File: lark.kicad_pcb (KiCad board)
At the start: 2 copper layers, 128 parts, among them CON1 SJ1-3523N, IC1 MS5611-01BA03, IC2 MS5611-01BA03, J1 SPI, J2 UART0, J3 I2C_0, J4 PWR_IN, J5 UE27AC54100, J6 UART1, J7 54602-908LF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

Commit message: Intermediate status while arranging compontents.
Manually grouped components into smaller islands.

Some parts were changed:
* U1: SOT-23-3 LDO should be sufficient
* CP_Elec: Use 10x10 size
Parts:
- C10, C16, C46: footprint Capacitor_SMD:CP_Elec_16x17.5 -> Capacitor_SMD:CP_Elec_10x10
- D3, D5: footprint Diode_SMD:D_SMC_Handsoldering -> Diode_SMD:D_SOD-123
- D4: footprint Diode_SMD:D_SMB_Handsoldering -> Diode_SMD:D_SOD-123
- J5: moved to B.Cu
- U1: value AP1117-33 -> MCP1700T-3302E_TT; footprint Package_TO_SOT_SMD:SOT-223-3_TabPin2 -> Package_TO_SOT_SMD:SOT-23
- U3, U4, U5, U6: footprint digikey-footprints:SOT-23-3 -> Package_TO_SOT_SMD:SOT-23
- moved C11 245.2 mm to (234.0, -23.0)
- moved C12 243.8 mm to (234.0, -27.0)
- moved C45 230.0 mm to (152.0, -50.0)
- moved C44 225.1 mm to (152.0, -54.0)
- moved C7 223.6 mm to (244.0, 119.0)
- moved R24 219.5 mm to (244.0, 122.0)
- moved C47 212.7 mm to (128.0, -56.5)
- moved R33 212.7 mm to (124.3, -54.5)
- moved R29 204.9 mm to (134.0, -46.0)
- moved R36 202.1 mm to (129.0, -50.0)
- moved C17 201.9 mm to (245.0, 63.0)
- moved C49 200.9 mm to (135.0, -50.0)
- moved R35 197.2 mm to (133.0, -38.0)
- moved R34 183.8 mm to (133.0, -41.0)
- moved U1 179.2 mm to (4.00, 70.0)
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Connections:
- IC1 pad 7: I2C1_SDA -> I2C0_SDA
- IC1 pad 8: I2C1_SCK -> I2C0_SCK
- IC2 pad 5: GND -> /Power/PDUSPWR
- U9 pad 6: I2C0_SDA -> I2C1_SDA
- U9 pad 7: I2C0_SCK -> I2C1_SCK

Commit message: continue layout work, WIP
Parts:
- moved J4 236.4 mm to (5.64, 7.74), turned to 270 degrees
- moved C10 236.0 mm to (7.00, -4.00), turned to 270 degrees
- moved D4 232.7 mm to (12.6, 5.74), turned to 180 degrees
- moved L1 230.2 mm to (17.6, -1.36)
- moved C9 227.7 mm to (20.6, -3.33)
- moved D3 225.7 mm to (18.6, 5.74), turned to 180 degrees
- moved RV1 225.1 mm to (15.4, 11.2), turned to 180 degrees
- moved C12 222.2 mm to (13.6, 1.62), turned to 270 degrees
- moved C8 222.1 mm to (20.6, 1.64), turned to 270 degrees
- moved C11 221.2 mm to (13.6, -3.36), turned to 90 degrees
- moved U2 212.4 mm to (28.0, 2.38), turned to 90 degrees
- moved C16 208.6 mm to (42.0, -5.00)
- moved D5 206.4 mm to (51.0, 6.00), turned to 90 degrees
- moved C17 204.4 mm to (51.0, -1.26), turned to 90 degrees
- moved L3 204.2 mm to (42.0, 8.00), turned to 180 degrees
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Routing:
- net I2C0_SCK: track 0.00 -> 44.7 mm
- net I2C0_SDA: track 0.00 -> 43.8 mm
- net I2C1_SCK: track 0.00 -> 24.8 mm
- net I2C1_SDA: track 0.00 -> 16.5 mm
- net BOOTM: track 0.00 -> 15.1 mm, vias 0 -> 1
- net SPICS0: track 0.00 -> 14.2 mm, vias 0 -> 1
- net U1TXD: track 0.00 -> 12.5 mm
- net U0RXD: track 0.00 -> 11.6 mm, vias 0 -> 1
- net SW_VARIO: track 0.00 -> 10.5 mm, vias 0 -> 1
- net U1RTS: track 0.00 -> 8.74 mm
- net SPID: track 0.00 -> 8.72 mm
- net U2TXD: track 0.00 -> 8.57 mm
- net SPIQ: track 0.00 -> 7.39 mm
- net U1CTS: track 0.00 -> 7.16 mm
- net SPICLK: track 0.00 -> 7.14 mm
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
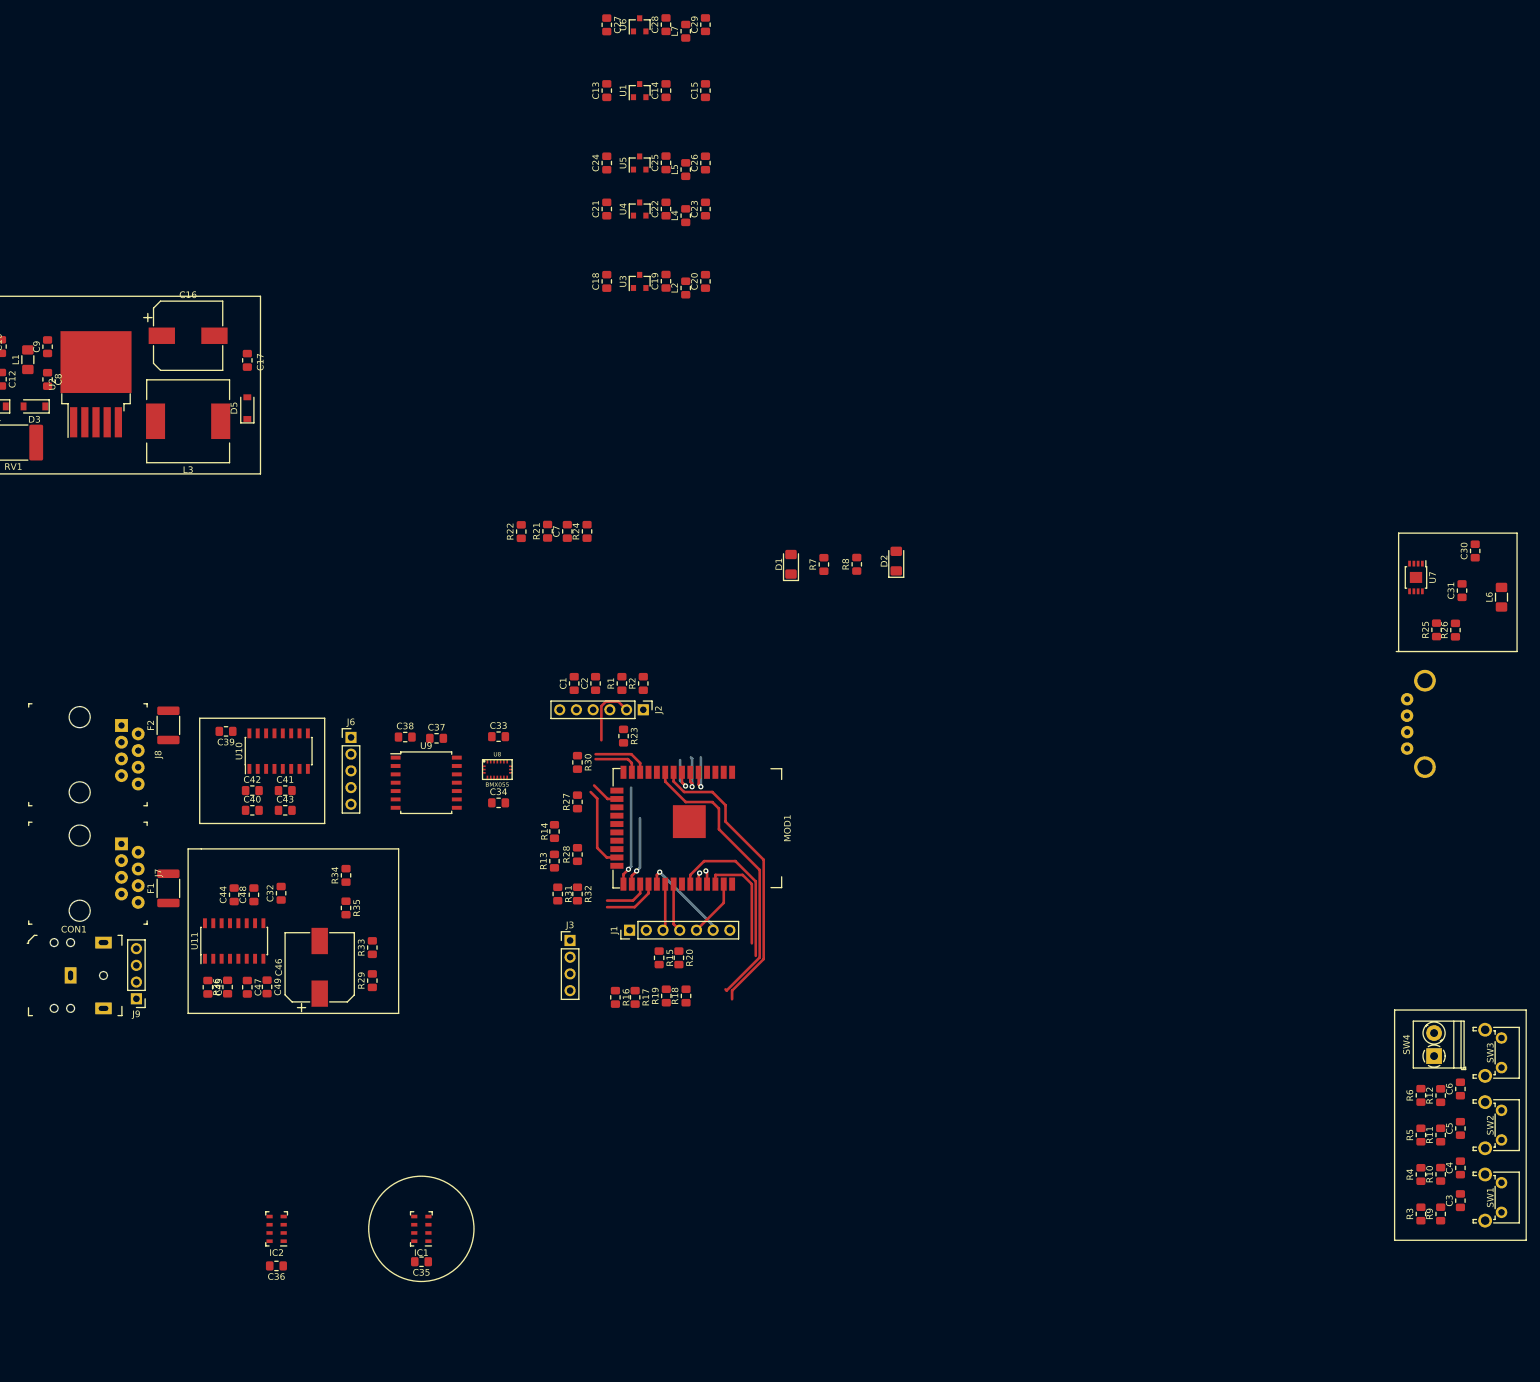
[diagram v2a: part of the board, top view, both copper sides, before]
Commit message: Updating schematic for the first prototype
* U1 can supply up to 600 mA
* drop USB charger for now
* smaller type of DC/DC (U2) for input
* remove one of the large capacitors
* change BMX interface to 4-wire SPI for speed reasons
* add I2C mux for pressure sensors

The changes were made during the meeting with Tomas.

BMX055 will be replaced by BMX088. For mechanical reasons, the pressure
sensors will be placed on a daughterboard. The daughterboard could get
footprints for different kinds pressure sensors (i.e. BMP388, HCLA0025).
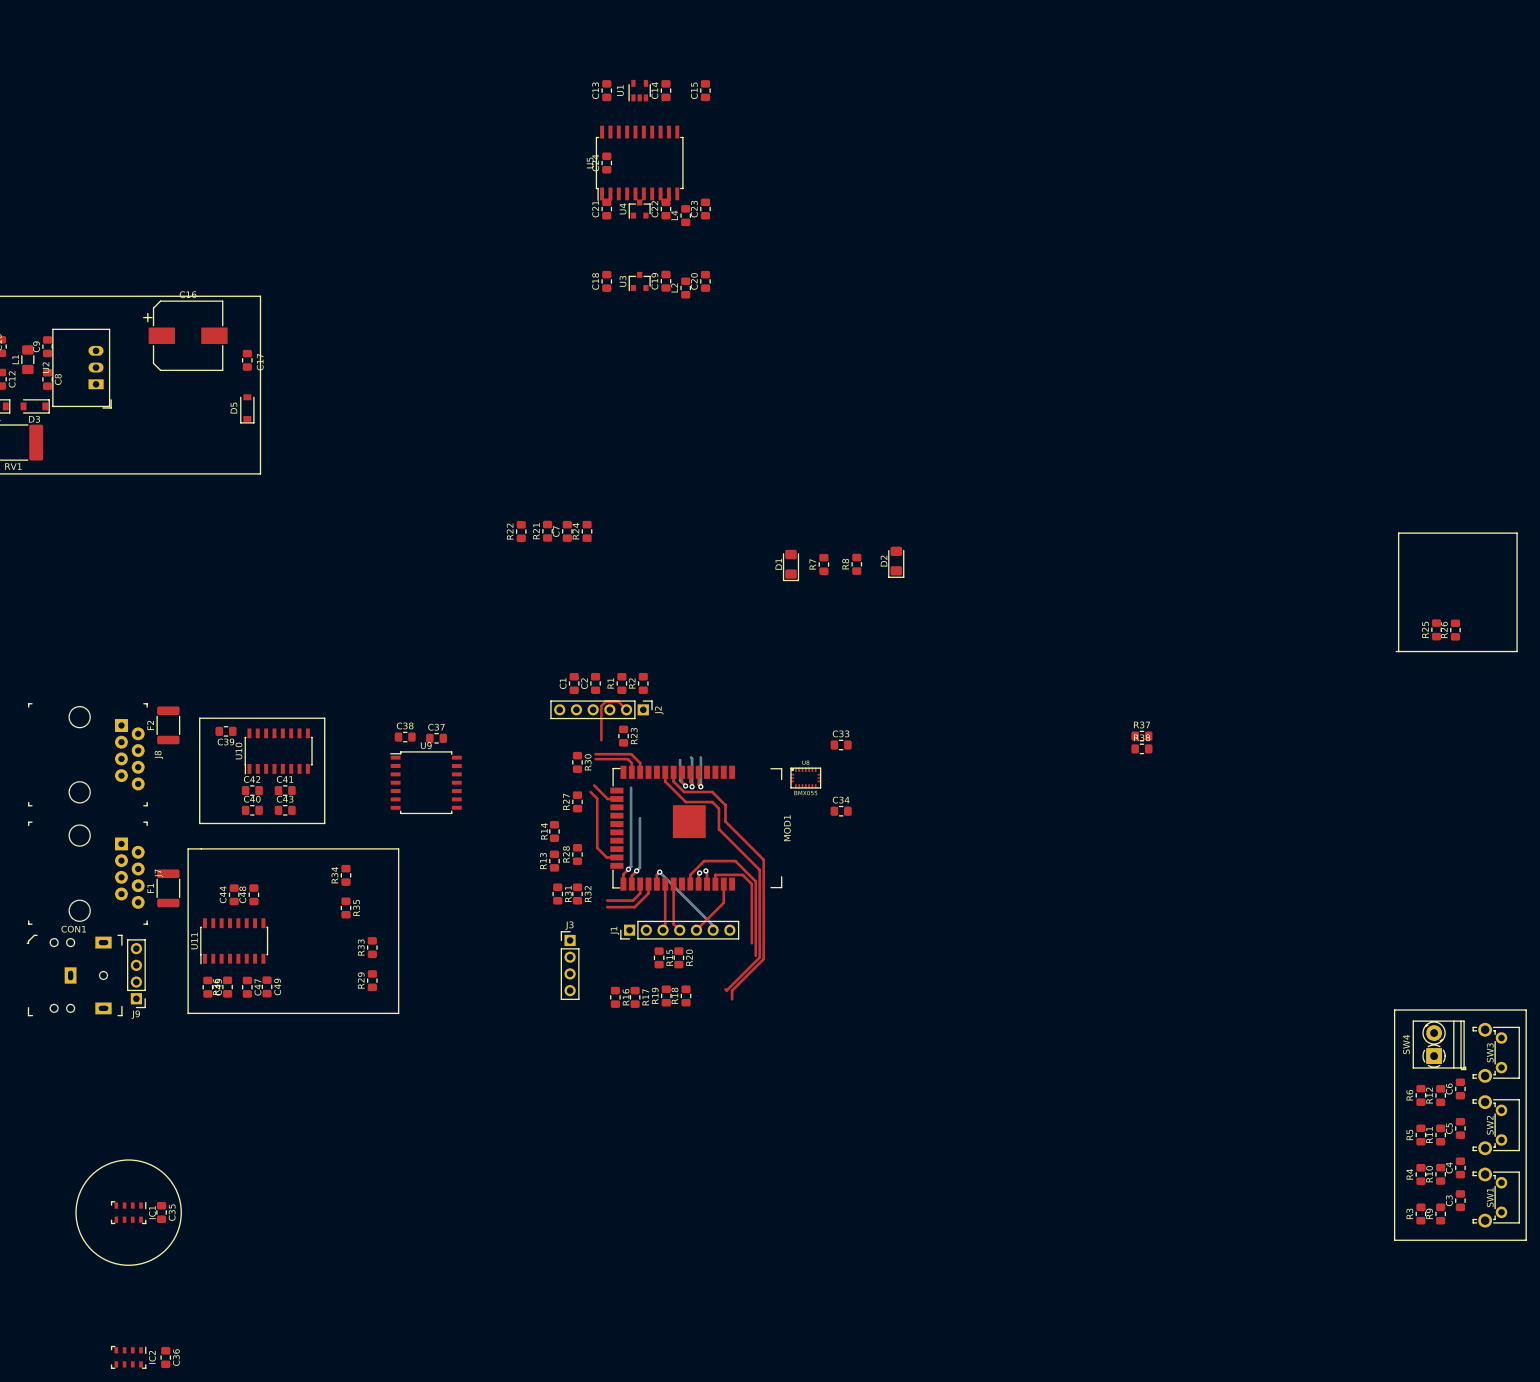
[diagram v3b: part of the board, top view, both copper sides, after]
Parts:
- removed C25, C26, C27, C28, C29, C31: 1u, Capacitor_SMD:C_0805_2012Metric_Pad1.15x1.40mm_HandSolder
- removed C30, C32: 100n, Capacitor_SMD:C_0805_2012Metric_Pad1.15x1.40mm_HandSolder
- removed C46: 470u, Capacitor_SMD:CP_Elec_10x10
- removed J5: UE27AC54100, digikey-footprints:USB_A_Female_UE27AC54100
- removed J6: UART1, Connector_PinHeader_2.54mm:PinHeader_1x05_P2.54mm_Vertical
- removed L3: 47uH/3.5A, Inductor_SMD:L_12x12mm_H8mm
- removed L5, L7: Ferrite_Bead, Inductor_SMD:L_0805_2012Metric_Pad1.15x1.40mm_HandSolder
- removed L6: Ferrite_Bead, Inductor_SMD:L_1206_3216Metric_Pad1.42x1.75mm_HandSolder
- removed U6: MCP1700T-3302E_TT, Package_TO_SOT_SMD:SOT-23
- removed U7: TPS2511, Package_SO:MSOP-8-1EP_3x3mm_P0.65mm_EP1.68x1.88mm
- added R37: 10k, Resistor_SMD:R_0805_2012Metric_Pad1.15x1.40mm_HandSolder, F.Cu at (187.0, 55.9)
- added R38: 10k, Resistor_SMD:R_0805_2012Metric_Pad1.15x1.40mm_HandSolder, F.Cu at (187.0, 57.8)
- C24: value 1u -> 100n
- R26: value 22k -> 10k
- R29, R30: value 470R -> 10k
- U1: value MCP1700T-3302E_TT -> AP2112K-3.3; footprint Package_TO_SOT_SMD:SOT-23 -> Package_TO_SOT_SMD:SOT-23-5
- U2: value LM2596S-5 -> R-785.0-1.0; footprint Package_TO_SOT_SMD:TO-263-5_TabPin3 -> Converter_DCDC:Converter_DCDC_RECOM_R-78E-0.5_THT
- U5: value MCP1700T-3302E_TT -> PCA9544AD; footprint Package_TO_SOT_SMD:SOT-23 -> Package_SO:SOIC-20W_7.5x12.8mm_P1.27mm
- moved C33 52.1 mm to (141.3, 57.2)
- moved C34 52.1 mm to (141.3, 67.3)
- moved U8 46.9 mm to (135.9, 62.2)
- moved IC1 44.6 mm to (33.0, 128.3), turned to 270 degrees
- moved C35 40.2 mm to (38.0, 128.3), turned to 270 degrees
- moved IC2 29.8 mm to (33.0, 150.3), turned to 270 degrees
- moved C36 21.8 mm to (38.6, 150.3), turned to 270 degrees
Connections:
- net Net-(U8-Pad16) renamed /Sensors/CS_ACC
- net Net-(U8-Pad5) renamed /Sensors/CS_GYR
- C23 pad 1: /Power/PSTATPWR -> /Power/SENSPWR
- C24 pad 1: +5V -> GND
- C24 pad 2: GND -> /Power/SENSPWR
- C35 pad 1: /Power/PSTATPWR -> GND
- C35 pad 2: GND -> /Power/SENSPWR
- C36 pad 1: /Power/PDUSPWR -> GND
- C36 pad 2: GND -> /Power/SENSPWR
- C37 pad 1: /Power/PDIFPWR -> /Power/SENSPWR
- C38 pad 1: /Power/PDIFPWR -> /Power/SENSPWR
- D5 pad 1: Net-(D5-Pad1) -> +12V
- D5 pad 2: GND -> +5V
- IC1 pad 1: /Power/PSTATPWR -> /Power/SENSPWR
- IC1 pad 2: /Power/PSTATPWR -> /Power/SENSPWR
- IC1 pad 4: GND -> /Power/SENSPWR
- IC1 pad 5: GND -> /Power/SENSPWR
- IC1 pad 7: I2C0_SDA -> Net-(IC1-Pad7)
- IC1 pad 8: I2C0_SCK -> Net-(IC1-Pad8)
- IC2 pad 1: /Power/PDUSPWR -> /Power/SENSPWR
- IC2 pad 2: /Power/PDUSPWR -> /Power/SENSPWR
- IC2 pad 4: GND -> /Power/SENSPWR
- IC2 pad 5: /Power/PDUSPWR -> /Power/SENSPWR
- IC2 pad 7: I2C0_SDA -> Net-(IC2-Pad7)
- IC2 pad 8: I2C0_SCK -> Net-(IC2-Pad8)
- L4 pad 1: /Power/PSTATPWR -> /Power/SENSPWR
- MOD1 pad 12: U1RTS -> INT_GYR
- MOD1 pad 13: U1CTS -> INT_ACC
- MOD1 pad 33: I2C1_SCK -> CS_ACC
- MOD1 pad 36: I2C1_SDA -> CS_GYR
- R16 pad 1: I2C1_SCK -> /Power/SENSPWR
- R16 pad 2: VDD -> Net-(R16-Pad2)
- R17 pad 1: I2C1_SDA -> /Power/SENSPWR
- R17 pad 2: VDD -> Net-(IC1-Pad7)
- R25 pad 1: Net-(R25-Pad1) -> /Power/SENSPWR
- R25 pad 2: +5V -> Net-(IC2-Pad7)
- R26 pad 1: Net-(R26-Pad1) -> /Power/SENSPWR
- R26 pad 2: GND -> Net-(R26-Pad2)
- R29 pad 1: Net-(J6-Pad3) -> /Power/SENSPWR
- R29 pad 2: U1RTS -> Net-(R29-Pad2)
- R30 pad 1: Net-(J6-Pad4) -> /Power/SENSPWR
- R30 pad 2: U1CTS -> Net-(IC1-Pad8)
- U1 pad 1: GND -> +5V
- U1 pad 2: VDD -> GND
- U2 pad 2: Net-(D5-Pad1) -> GND
- U2 pad 3: GND -> +5V
- U5 pad 2: Net-(C25-Pad1) -> GND
- U5 pad 3: +5V -> GND
- U8 pad 11: I2C1_SDA -> SPID
- U8 pad 12: GND -> SPIQ
- U8 pad 17: GND -> SPIQ
- U8 pad 20: GND -> Net-(U8-Pad20)
- U8 pad 9: I2C1_SCK -> SPICLK
- U9 pad 10: /Power/PDIFPWR -> /Power/SENSPWR
- U9 pad 11: /Power/PDIFPWR -> /Power/SENSPWR
- U9 pad 13: /Power/PDIFPWR -> /Power/SENSPWR
- U9 pad 6: I2C1_SDA -> Net-(R26-Pad2)
- U9 pad 7: I2C1_SCK -> Net-(R38-Pad2)
- U9 pad 8: /Power/PDIFPWR -> /Power/SENSPWR
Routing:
- net I2C1_SCK: track 24.8 -> 0.00 mm
- net CS_ACC: track 0.00 -> 24.8 mm
- net I2C1_SDA: track 16.5 -> 0.00 mm
- net CS_GYR: track 0.00 -> 16.5 mm
- net U1RTS: track 8.74 -> 0.00 mm
- net INT_GYR: track 0.00 -> 8.74 mm
- net U1CTS: track 7.16 -> 0.00 mm
- net INT_ACC: track 0.00 -> 7.16 mm

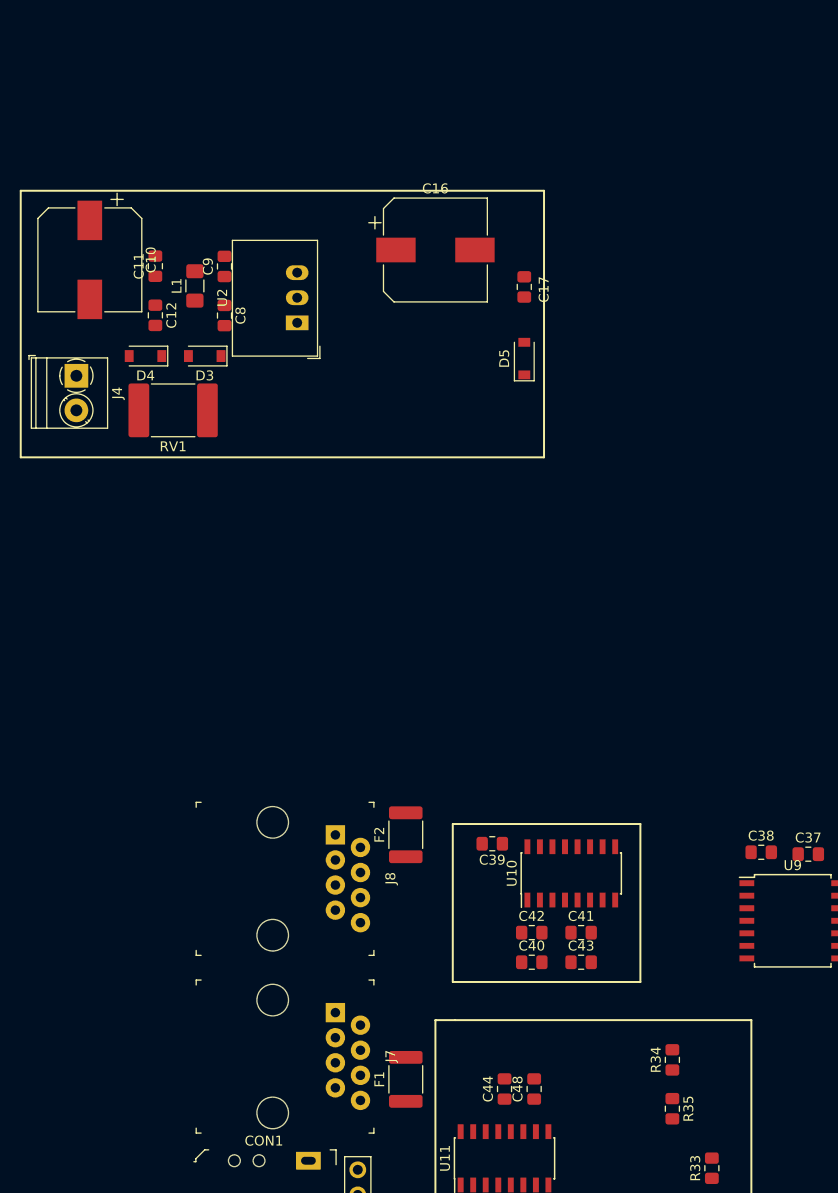
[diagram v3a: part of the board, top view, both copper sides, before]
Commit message: Use BMI088 instead of BMX055.
Symbol for BMI088 was created and placed in the schematic.

Still looking for a LGA-16 4.5x3.0 footprint. Do we really need to
create that ourselves?
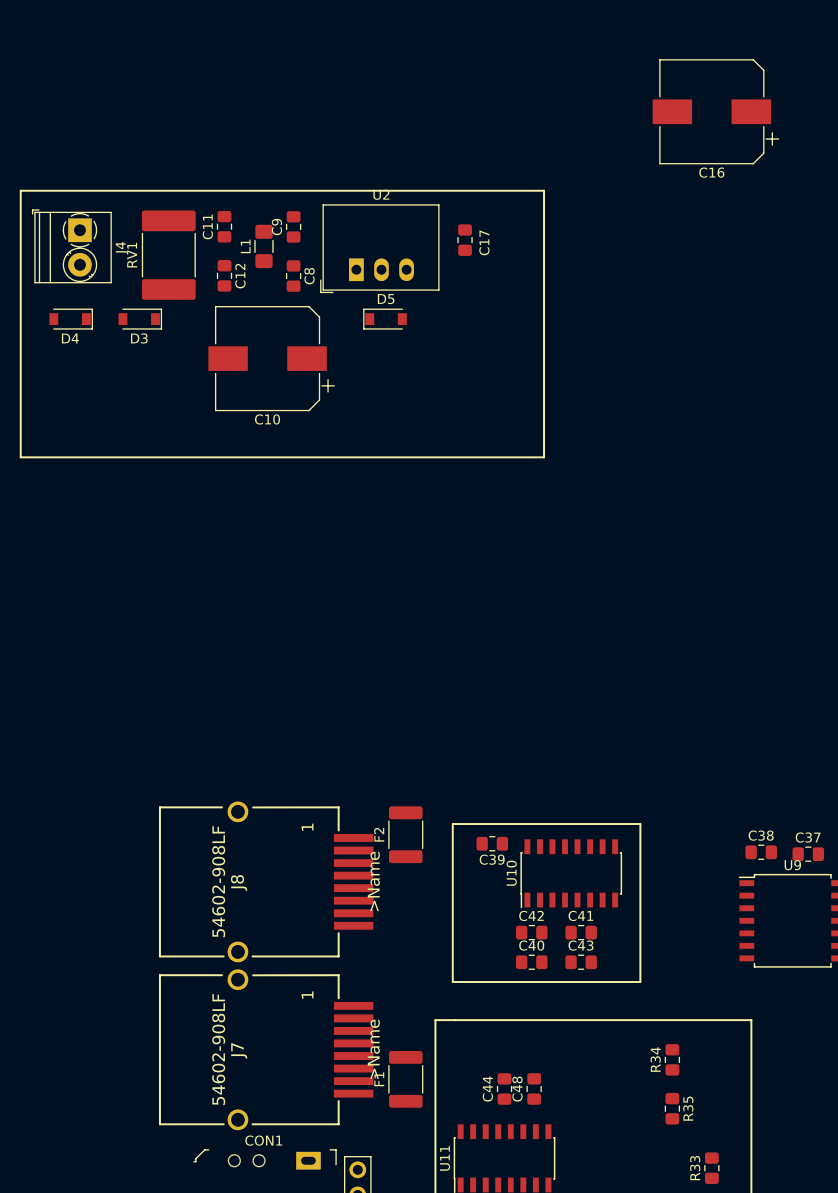
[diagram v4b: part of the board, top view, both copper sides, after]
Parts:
- J7, J8: footprint digikey-footprints:Ethernet_Jack_54602-908LF -> libs:634108185521
- moved C16 31.3 mm to (70.0, -19.0), turned to 180 degrees
- moved C10 20.6 mm to (25.0, 6.00), turned to 180 degrees
- moved RV1 15.7 mm to (15.0, -4.47), turned to 90 degrees
- moved J4 14.7 mm to (6.00, -7.00)
- moved D5 14.6 mm to (37.0, 2.00), turned to 0 degrees
- moved J8 11.0 mm to (22.0, 59.0)
- moved J7 10.6 mm to (22.0, 76.0)
- moved D4 8.50 mm to (5.00, 2.00)
- moved C8 8.06 mm to (27.6, -2.36)
- moved C9 8.06 mm to (27.6, -7.33)
- moved L1 8.06 mm to (24.6, -5.36)
- moved C11 8.06 mm to (20.6, -7.36)
- moved C12 8.06 mm to (20.6, -2.38)
- moved U2 8.06 mm to (34.0, -3.00), turned to 0 degrees
- moved C17 7.65 mm to (45.0, -6.00)
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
